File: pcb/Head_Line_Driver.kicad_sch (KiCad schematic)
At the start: 12 parts

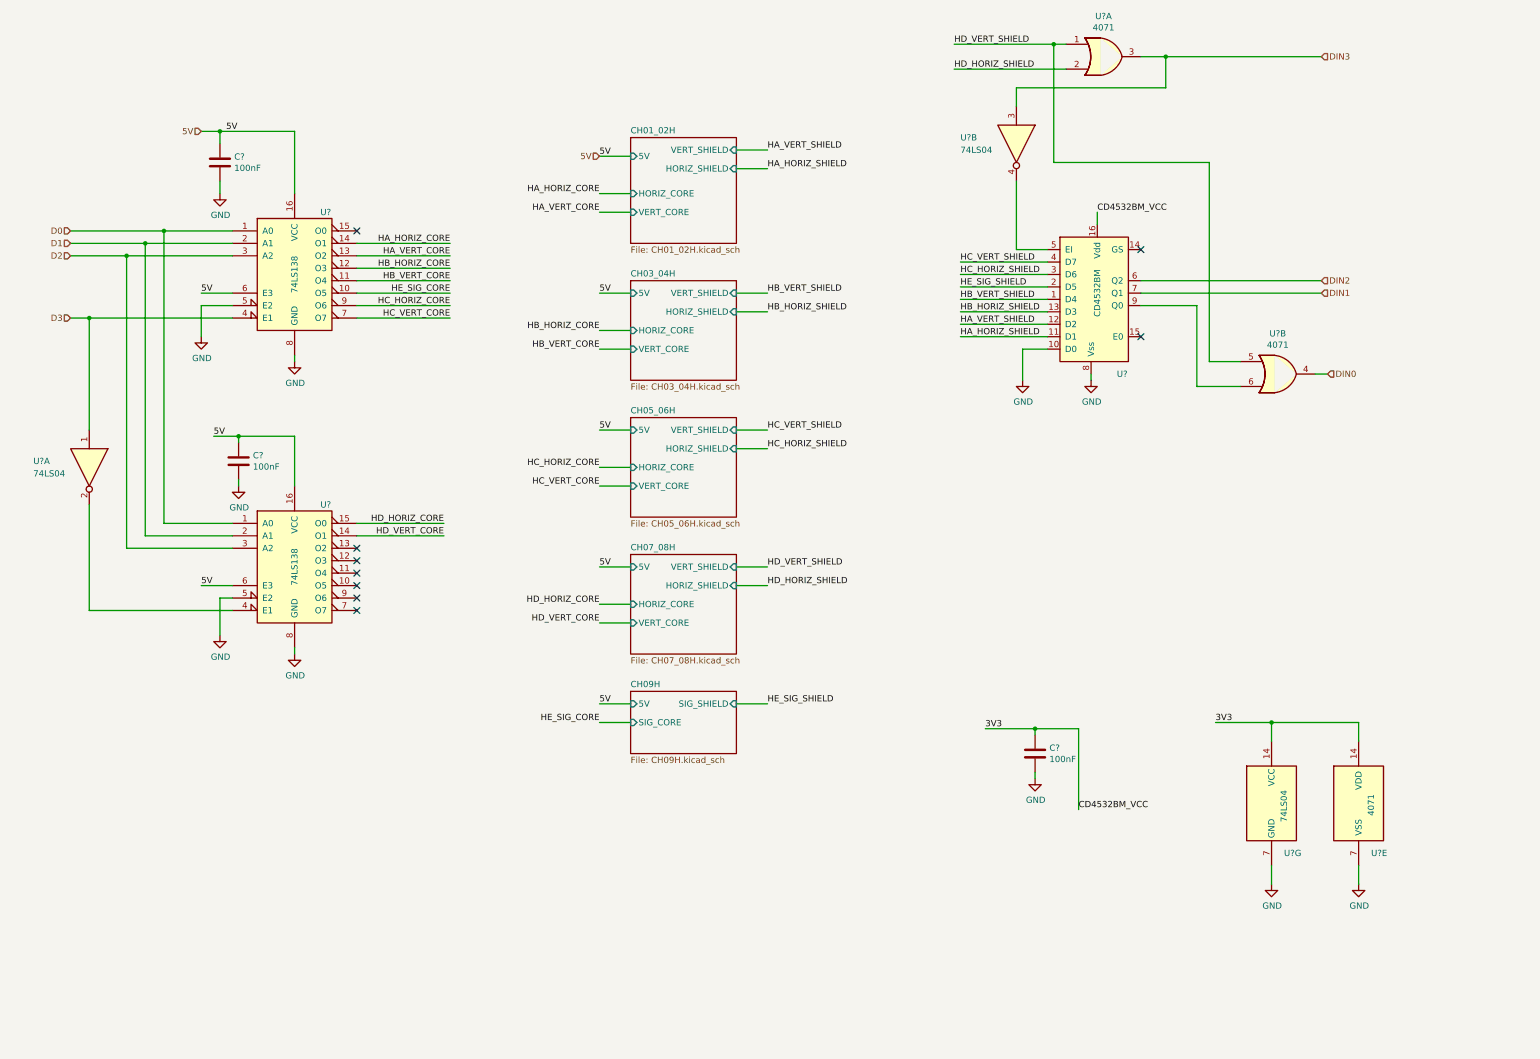
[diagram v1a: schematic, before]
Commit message: Introduces shift registers in the coax driver
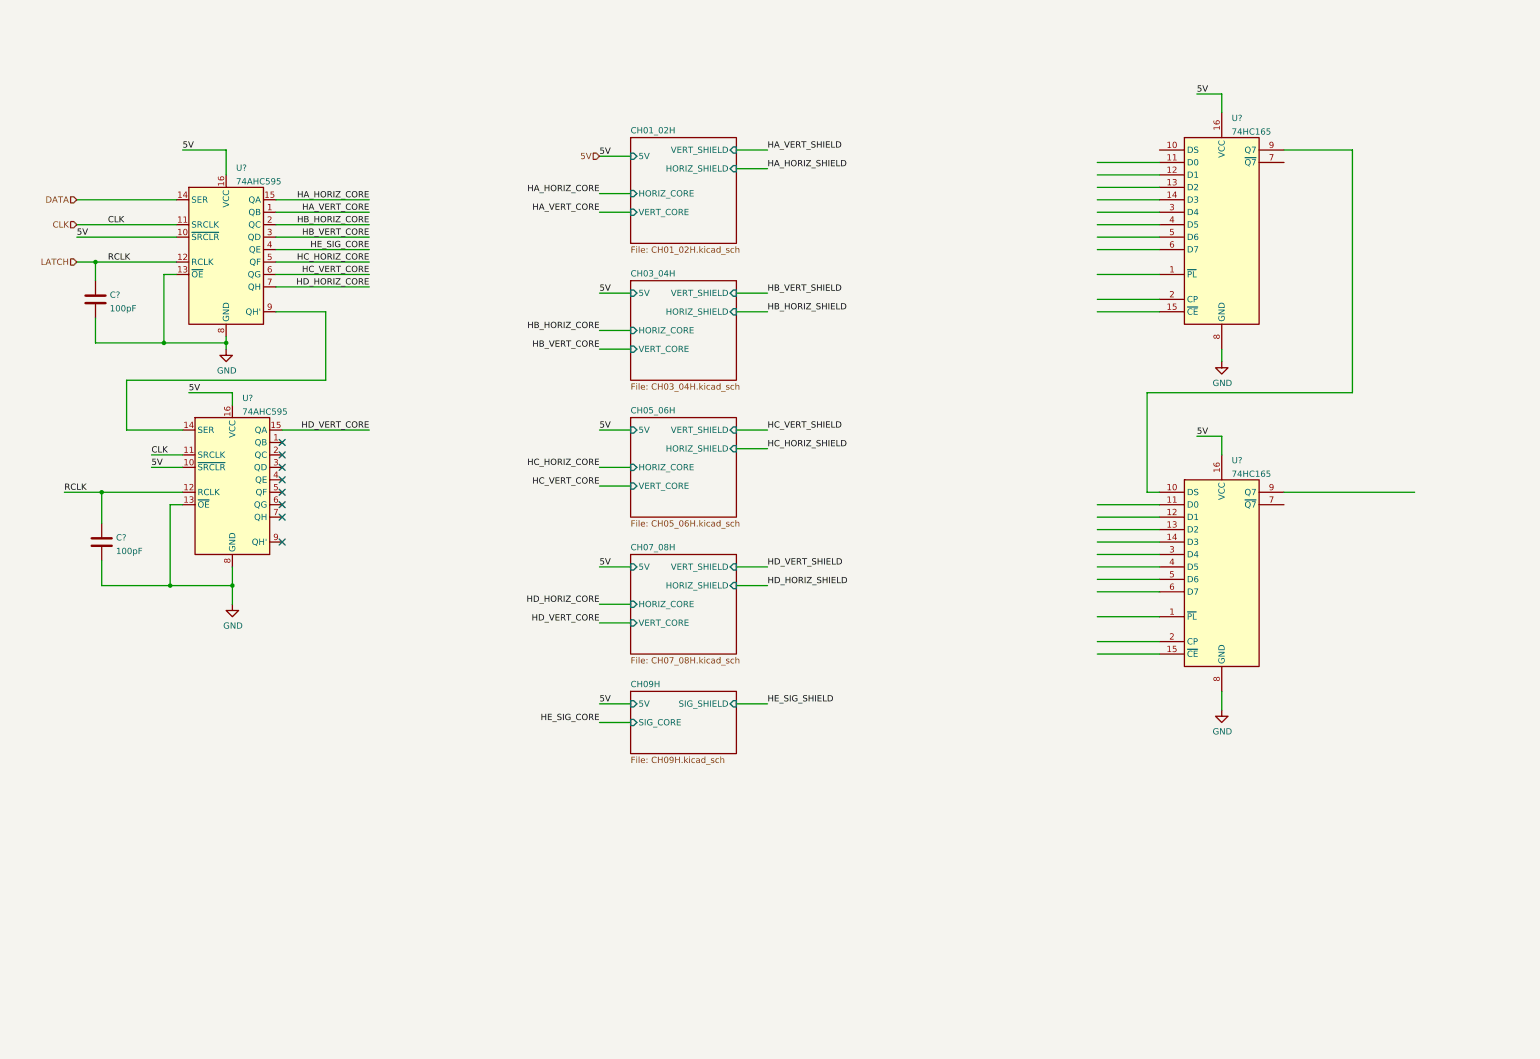
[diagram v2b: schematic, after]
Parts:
- removed C? (x3): 100nF, Capacitor_SMD:C_0805_2012Metric, symbol Device:C
- removed U? (x2): 74LS138, soic:SOIC-16, symbol 74xx:74LS138
- removed U?: CD4532BM, Package_SO:SO-16_3.9x9.9mm_P1.27mm, symbol CoaxTester:CD4532BM
- removed U? (x3): 74LS04, LED_Chain:SOIC-14, symbol 74xx:74LS04
- removed U? (x3): 4071, LED_Chain:SOIC-14, symbol 4xxx:4071
- added C? (x2): 100pF, symbol Device:C
- added U? (x2): 74AHC595, symbol 74xx:74AHC595
- added U? (x2): 74HC165, symbol 74xx:74HC165
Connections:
- net 5V: now also U?.10 (~{SRCLR}), U?.10 (~{SRCLR}), U?.16 (VCC), U?.16 (VCC), U?.16 (VCC), U?.16 (VCC)
- net GND: now also C?.2, C?.2, U?.13 (~{OE}), U?.13 (~{OE}), U?.8 (GND), U?.8 (GND), U?.8 (GND), U?.8 (GND)
- net HA_HORIZ_CORE: now also U?.15 (QA)
- net HA_VERT_CORE: now also U?.1 (QB)
- net HB_HORIZ_CORE: now also U?.2 (QC)
- net HB_VERT_CORE: now also U?.3 (QD)
- net HC_HORIZ_CORE: now also U?.5 (QF)
- net HC_VERT_CORE: now also U?.6 (QG)
- net HD_HORIZ_CORE: now also U?.7 (QH)
- net HD_VERT_CORE: now also U?.15 (QA)
- net HE_SIG_CORE: now also U?.4 (QE)
- new net: U?.14 (SER), U?.9 (QH')
- new net: U?.10 (DS), U?.9 (Q7)
- new net CLK: U?.11 (SRCLK), U?.11 (SRCLK)
- new net DATA: U?.14 (SER)
- new net LATCH: C?.1, C?.1, U?.12 (RCLK), U?.12 (RCLK)
- no-connect marks 9 -> 8

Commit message: Shift register updates - changes the driver from pnp to npn
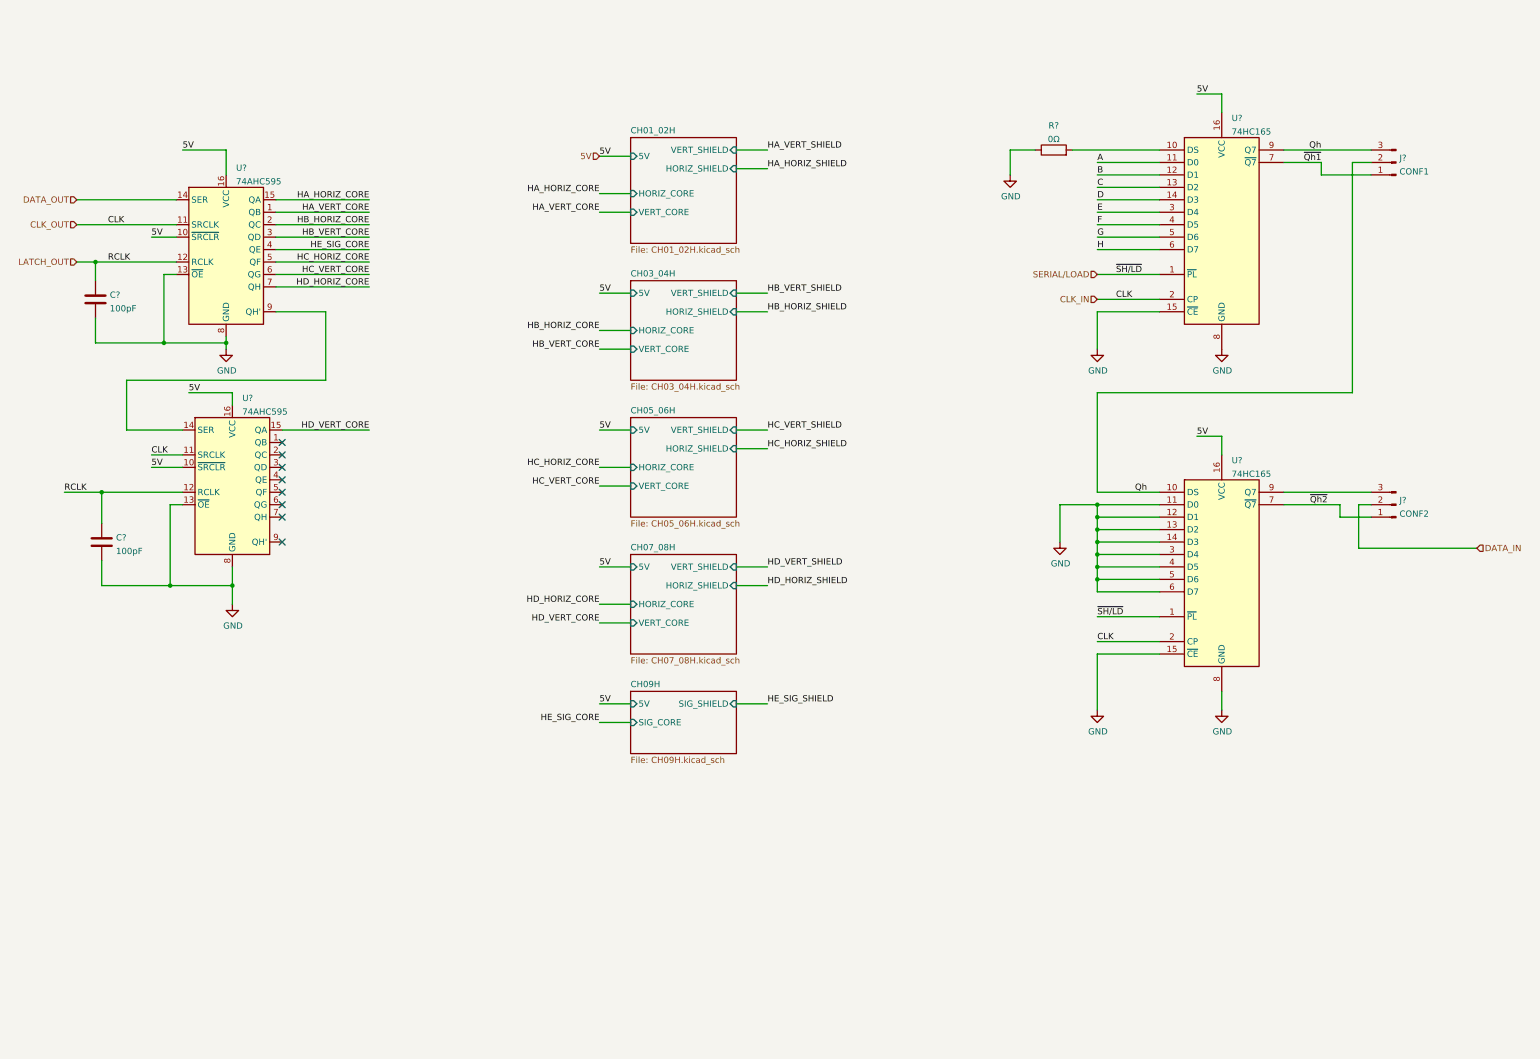
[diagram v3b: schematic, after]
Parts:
- added J?: CONF1, symbol Connector:Conn_01x03_Male
- added J?: CONF2, symbol Connector:Conn_01x03_Male
- added R?: 0Ω, symbol Device:R
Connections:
- net CLK is gone; now on net CLK_IN: U?.11 (SRCLK), U?.11 (SRCLK)
- net GND: now also U?.11 (D0), U?.12 (D1), U?.13 (D2), U?.14 (D3), U?.15 (~{CE}), U?.15 (~{CE}), U?.3 (D4), U?.4 (D5), U?.5 (D6), U?.6 (D7), R?.1
- net SERIAL/LOAD: now reaches U?.1 (~{PL})
- net SERIAL/LOAD: now also U?.1 (~{PL})
- net Qh: now reaches U?.10 (DS), U?.9 (Q7)
- net Qh: now also J?.2 (Pin_2), J?.3 (Pin_3)
- net CLK_IN: now reaches U?.2 (CP)
- net CLK_IN: now also U?.2 (CP)
- net ~{Qh2}: now reaches U?.7 (~{Q7})
- net ~{Qh2}: now also J?.1 (Pin_1)
- net at U?.9 (Q7): now also J?.3 (Pin_3)
- net at U?.10 (DS): now also R?.2
- net A: now reaches U?.11 (D0)
- net B: now reaches U?.12 (D1)
- net C: now reaches U?.13 (D2)
- net D: now reaches U?.14 (D3)
- net E: now reaches U?.3 (D4)
- net F: now reaches U?.4 (D5)
- net G: now reaches U?.5 (D6)
- net H: now reaches U?.6 (D7)
- net ~{Qh1}: now reaches U?.7 (~{Q7})
- net ~{Qh1}: now also J?.1 (Pin_1)
- net DATA renamed DATA_OUT
- net LATCH renamed LATCH_OUT
- new net DATA_IN: J?.2 (Pin_2)

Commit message: Updates to the shematic for mechanics
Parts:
- C? (x2): footprint (none) -> Capacitor_SMD:C_0805_2012Metric
- J? (x2): footprint (none) -> Jumper:SolderJumper-3_P1.3mm_Bridged12_RoundedPad1.0x1.5mm
- R?: footprint (none) -> Resistor_SMD:R_0805_2012Metric
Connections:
- net A is gone; now on net HA_VERT_SHIELD: U?.11 (D0)
- net B is gone; now on net HA_HORIZ_SHIELD: U?.12 (D1)
- net C is gone; now on net HB_VERT_SHIELD: U?.13 (D2)
- net D is gone; now on net HB_HORIZ_SHIELD: U?.14 (D3)
- net E is gone; now on net HE_SIG_SHIELD: U?.3 (D4)
- net F is gone; now on net HC_VERT_SHIELD: U?.4 (D5)
- net G is gone; now on net HC_HORIZ_SHIELD: U?.5 (D6)
- net H is gone; now on net HD_VERT_SHIELD: U?.6 (D7)
- net GND: no longer U?.11 (D0)
- net HD_HORIZ_SHIELD: now also U?.11 (D0)
- net Qh: now also J?.1 (Pin_1); no longer J?.3 (Pin_3)
- net ~{Qh1}: now also J?.3 (Pin_3); no longer J?.1 (Pin_1)
- net ~{Qh2}: now also J?.3 (Pin_3); no longer J?.1 (Pin_1)
- net at U?.9 (Q7): now also J?.1 (Pin_1); no longer J?.3 (Pin_3)
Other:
- note added: "Each module connects to an F-Connector The output from the 74HC595 goes to the core and the input from the shield goes to the 75HC165. In addition, there is a voltage divider incase the return voltage needs to be stepped down."
- note added: "Output Configuration Solder bridge to select between Qh and ~{Qh}"
- note added: "Q: Will there be any transmission effects? i.e. by sending the signal down a possibly 20m cable. It is not inteded to be a pulse but a purely a change in state."
- moved on the sheet: C?, J?, R?, U?

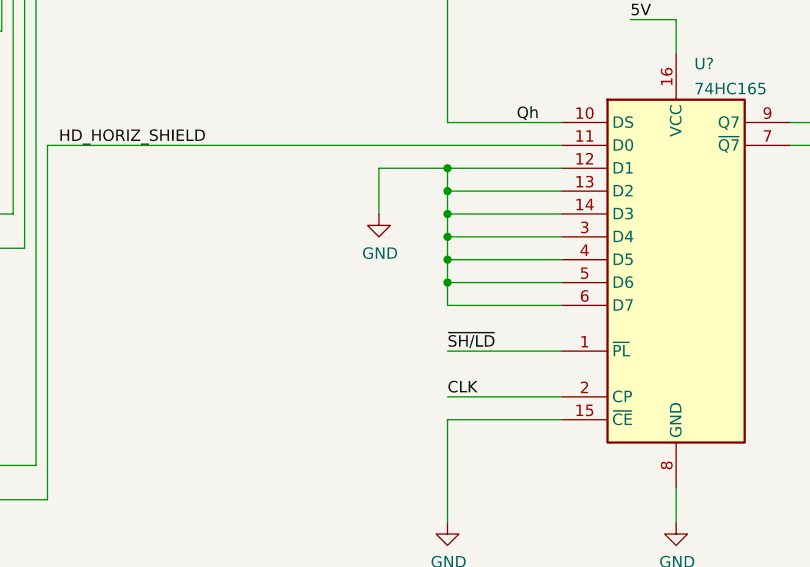
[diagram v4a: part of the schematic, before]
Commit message: Proof of concept for XBee tail unit. Correction to XBee symbol
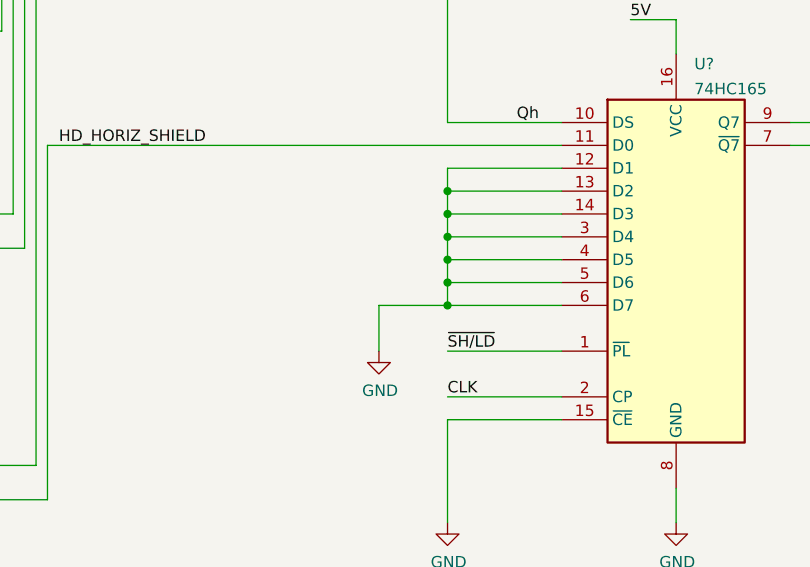
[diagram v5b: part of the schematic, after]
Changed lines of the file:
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@@
 (kicad_sch (version 20211123) (generator eeschema)
   (paper "A3")
+  (junction (at 265.43 171.45) (diameter 0) (color 0 0 0 0)
+  )
   (junction (at 265.43 163.83) (diameter 0) (color 0 0 0 0)
   )
@@
   )
   (junction (at 95.25 106.68) (diameter 0) (color 0 0 0 0)
-  )
-  (junction (at 265.43 156.21) (diameter 0) (color 0 0 0 0)
   )
   (junction (at 265.43 158.75) (diameter 0) (color 0 0 0 0)
@@
     (stroke (width 0) (type default) (color 0 0 0 0))
   )
-  (wire (pts (xy 257.81 156.21) (xy 265.43 156.21))
-    (stroke (width 0) (type default) (color 0 0 0 0))
-  )
   (wire (pts (xy 121.92 88.9) (xy 121.92 83.82))
     (stroke (width 0) (type default) (color 0 0 0 0))
@@
     (stroke (width 0) (type default) (color 0 0 0 0))
   )
-  (wire (pts (xy 257.81 161.29) (xy 257.81 156.21))
+  (wire (pts (xy 257.81 176.53) (xy 257.81 171.45))
     (stroke (width 0) (type default) (color 0 0 0 0))
   )
@@
   )
   (wire (pts (xy 265.43 166.37) (xy 265.43 168.91))
+    (stroke (width 0) (type default) (color 0 0 0 0))
+  )
+  (wire (pts (xy 257.81 171.45) (xy 265.43 171.45))
     (stroke (width 0) (type default) (color 0 0 0 0))
   )
@@
     (pin "1")
   )
-  (symbol (lib_id "power:GND") (at 257.81 161.29 0) (unit 1)
+  (symbol (lib_id "power:GND") (at 257.81 176.53 0) (unit 1)
     (in_bom yes) (on_board yes)
-    (property "Reference" "#PWR?" (id 0) (at 257.81 167.64 0)
-      (effects (font (size 1.27 1.27)) hide)
-    )
-    (property "Value" "GND" (id 1) (at 257.937 165.6842 0))
-    (property "Footprint" "" (id 2) (at 257.81 161.29 0)
-      (effects (font (size 1.27 1.27)) hide)
-    )
-    (property "Datasheet" "" (id 3) (at 257.81 161.29 0)
-      (effects (font (size 1.27 1.27)) hide)
-    )
+    (property "Reference" "#PWR?" (id 0) (at 257.81 182.88 0)
+      (effects (font (size 1.27 1.27)) hide)
+    )
+    (property "Value" "GND" (id 1) (at 257.937 180.9242 0))
+    (property "Footprint" "" (id 2) (at 257.81 176.53 0)
+      (effects (font (size 1.27 1.27)) hide)
+    )
+    (property "Datasheet" "" (id 3) (at 257.81 176.53 0)
+      (effects (font (size 1.27 1.27)) hide)
+    )

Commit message: Adds line protection
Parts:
- U? (x4): footprint (none) -> Package_SO:SO-16_3.9x9.9mm_P1.27mm
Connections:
- net HA_HORIZ_SHIELD: now also U?.11 (D0); no longer U?.12 (D1)
- net HA_VERT_SHIELD: now also U?.12 (D1); no longer U?.11 (D0)
- net HB_HORIZ_SHIELD: now also U?.13 (D2); no longer U?.14 (D3)
- net HB_VERT_SHIELD: now also U?.14 (D3); no longer U?.13 (D2)
- net HC_HORIZ_SHIELD: now also U?.4 (D5); no longer U?.5 (D6)
- net HC_VERT_SHIELD: now also U?.5 (D6); no longer U?.4 (D5)
- net HD_HORIZ_SHIELD: now also U?.6 (D7); no longer U?.11 (D0)
- net HD_VERT_SHIELD: now also U?.11 (D0); no longer U?.6 (D7)
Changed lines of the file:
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@@
     (stroke (width 0) (type default) (color 0 0 0 0))
   )
-  (wire (pts (xy 314.96 156.21) (xy 321.31 156.21))
+  (wire (pts (xy 312.42 156.21) (xy 321.31 156.21))
     (stroke (width 0) (type default) (color 0 0 0 0))
   )
@@
     (stroke (width 0) (type default) (color 0 0 0 0))
   )
-  (wire (pts (xy 303.53 153.67) (xy 314.96 153.67))
+  (wire (pts (xy 303.53 153.67) (xy 312.42 153.67))
     (stroke (width 0) (type default) (color 0 0 0 0))
   )
@@
     (stroke (width 0) (type default) (color 0 0 0 0))
   )
-  (wire (pts (xy 314.96 153.67) (xy 314.96 156.21))
+  (wire (pts (xy 312.42 153.67) (xy 312.42 156.21))
     (stroke (width 0) (type default) (color 0 0 0 0))
   )
@@
     (effects (font (size 1.27 1.27)) (justify left bottom))
   )
-  (label "HC_VERT_SHIELD" (at 222.25 96.52 0)
+  (label "HC_VERT_SHIELD" (at 222.25 99.06 0)
     (effects (font (size 1.27 1.27)) (justify left bottom))
   )
@@
     (effects (font (size 1.27 1.27)) (justify left bottom))
   )
-  (label "HB_VERT_SHIELD" (at 222.25 88.9 0)
+  (label "HB_VERT_SHIELD" (at 222.25 91.44 0)
     (effects (font (size 1.27 1.27)) (justify left bottom))
   )
@@
     (effects (font (size 1.27 1.27)) (justify left bottom))
   )
-  (label "HB_HORIZ_SHIELD" (at 222.25 91.44 0)
+  (label "HB_HORIZ_SHIELD" (at 222.25 88.9 0)
     (effects (font (size 1.27 1.27)) (justify left bottom))
   )
@@
     (effects (font (size 1.27 1.27)) (justify right bottom))
   )
-  (label "HA_VERT_SHIELD" (at 222.25 83.82 0)
+  (label "HA_VERT_SHIELD" (at 222.25 86.36 0)
     (effects (font (size 1.27 1.27)) (justify left bottom))
   )
@@
     (effects (font (size 1.27 1.27)) (justify left bottom))
   )
-  (label "HC_HORIZ_SHIELD" (at 222.25 99.06 0)
-    (effects (font (size 1.27 1.27)) (justify left bottom))
-  )
-  (label "HD_VERT_SHIELD" (at 222.25 101.6 0)
-    (effects (font (size 1.27 1.27)) (justify left bottom))
-  )
-  (label "HA_HORIZ_SHIELD" (at 222.25 86.36 0)
+  (label "HC_HORIZ_SHIELD" (at 222.25 96.52 0)
+    (effects (font (size 1.27 1.27)) (justify left bottom))
+  )
+  (label "HD_VERT_SHIELD" (at 222.25 153.67 0)
+    (effects (font (size 1.27 1.27)) (justify left bottom))
+  )
+  (label "HA_HORIZ_SHIELD" (at 222.25 83.82 0)
     (effects (font (size 1.27 1.27)) (justify left bottom))
   )
@@
     (effects (font (size 1.27 1.27)) (justify right bottom))
   )
-  (label "HD_HORIZ_SHIELD" (at 222.25 153.67 0)
+  (label "HD_HORIZ_SHIELD" (at 222.25 101.6 0)
     (effects (font (size 1.27 1.27)) (justify left bottom))
   )
@@
       (effects (font (size 1.27 1.27)) (justify left))
     )
-    (property "Footprint" "" (id 2) (at 123.19 151.13 0)
+    (property "Footprint" "Package_SO:SO-16_3.9x9.9mm_P1.27mm" (id 2) (at 123.19 151.13 0)
       (effects (font (size 1.27 1.27)) hide)
     )
@@
       (effects (font (size 1.27 1.27)) (justify left))
     )
-    (property "Footprint" "" (id 2) (at 290.83 166.37 0)
+    (property "Footprint" "Package_SO:SO-16_3.9x9.9mm_P1.27mm" (id 2) (at 290.83 166.37 0)
       (effects (font (size 1.27 1.27)) hide)
     )
@@
       (effects (font (size 1.27 1.27)) (justify left))
     )
-    (property "Footprint" "" (id 2) (at 290.83 96.52 0)
+    (property "Footprint" "Package_SO:SO-16_3.9x9.9mm_P1.27mm" (id 2) (at 290.83 96.52 0)
       (effects (font (size 1.27 1.27)) hide)
     )
@@
       (effects (font (size 1.27 1.27)) (justify left))
     )
-    (property "Footprint" "" (id 2) (at 121.92 104.14 0)
-      (effects (font (size 1.27 1.27)) hide)
-    )
+    (property "Footprint" "Package_SO:SO-16_3.9x9.9mm_P1.27mm" (id 2) (at 121.92 104.14 0)
+      (effects (font (size 1.27 1.27)) hide)
+    )
